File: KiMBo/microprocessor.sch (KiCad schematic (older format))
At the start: 44 parts

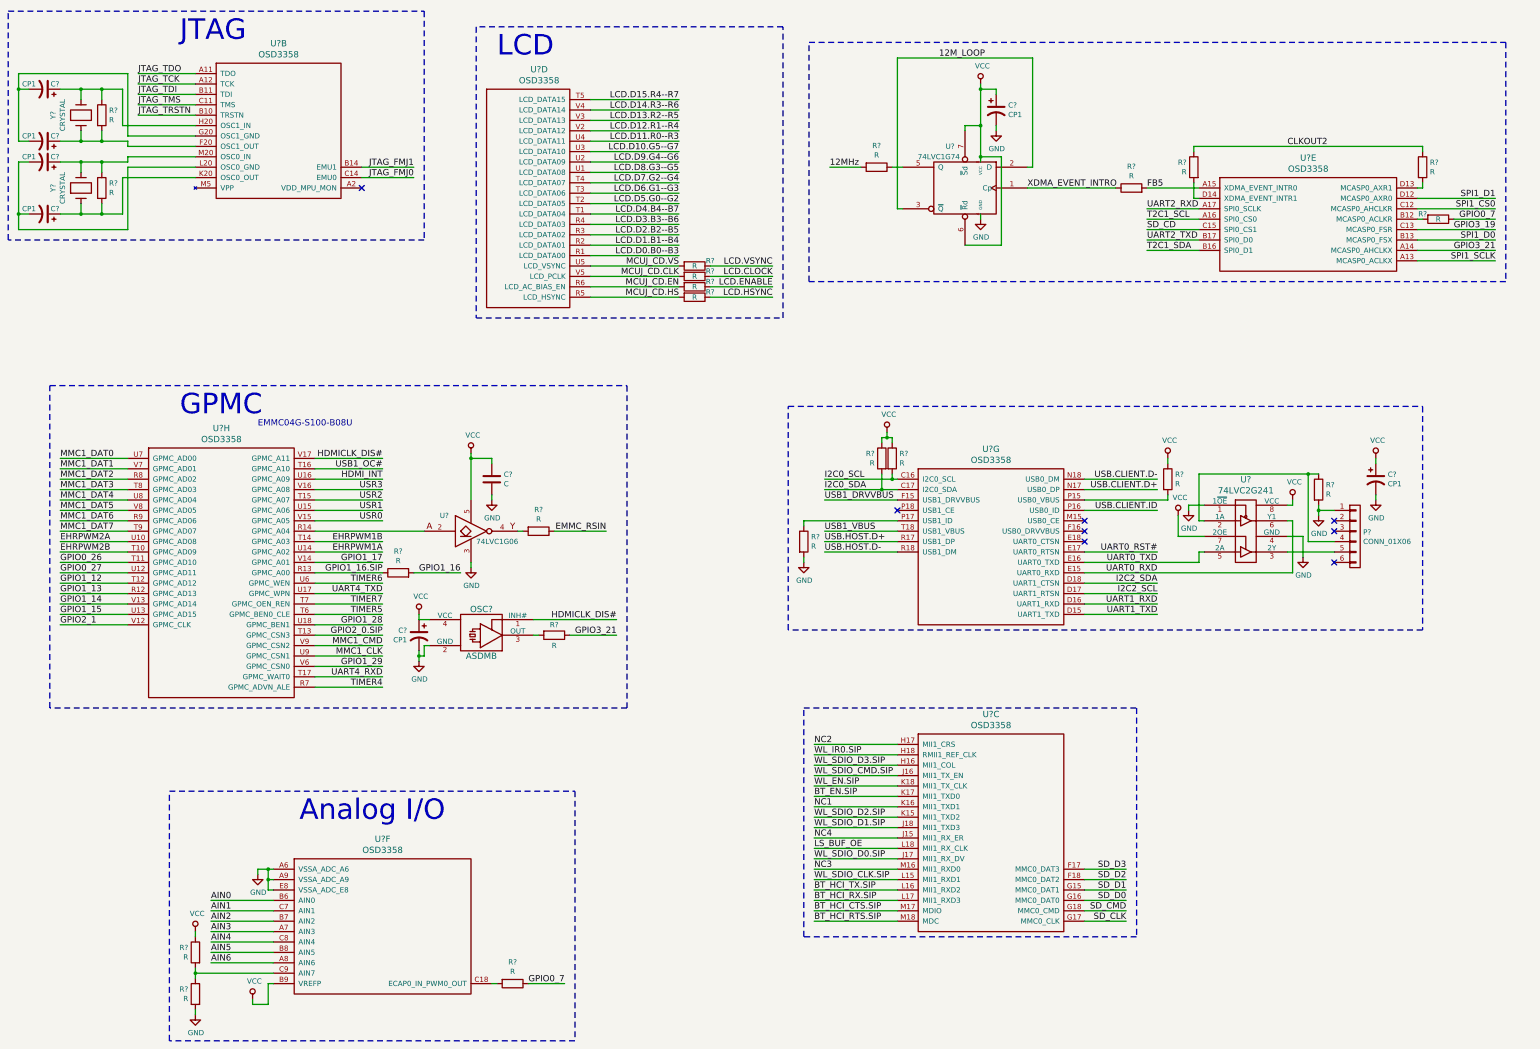
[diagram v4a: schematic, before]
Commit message: Add eMMC to the schematic
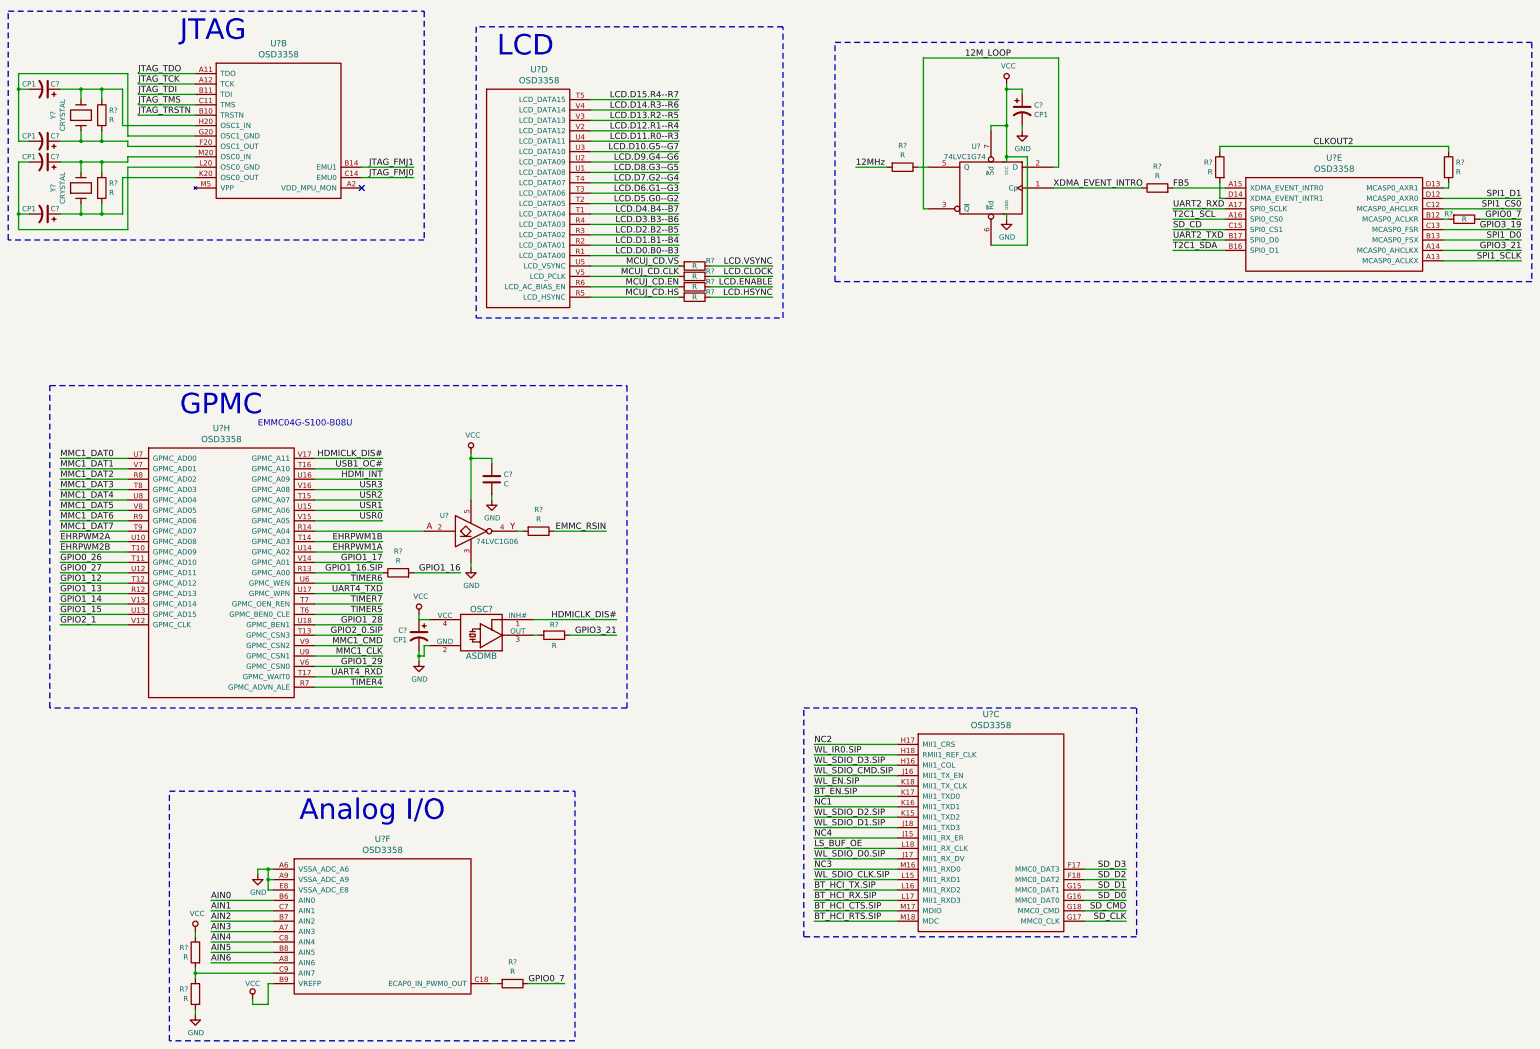
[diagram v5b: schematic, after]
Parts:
- removed C?: CP1, symbol CP1
- removed P?: CONN_01X06, symbol CONN_01X06
- removed R? (x5): R, symbol R
- removed U?: OSD3358, symbol OSD3358
- removed U?: 74LVC2G241, symbol 74LVC2G241
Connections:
- no-connect marks 8 -> 1
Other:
- moved on the sheet: C?, R?, U?, U?E
